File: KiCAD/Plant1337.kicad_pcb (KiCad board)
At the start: 4 copper layers, 59.6 x 48.3 mm, 61 parts, among them J1 USB_C_Receptacle_USB2.0_16P, Q1 AO3400A, Q2 AO3400A, Q3 AO3400A, Q4 AO3400A, U1 SHTC3, U2 ESP32-S3-WROOM-1, U3 AMS1117-3.3

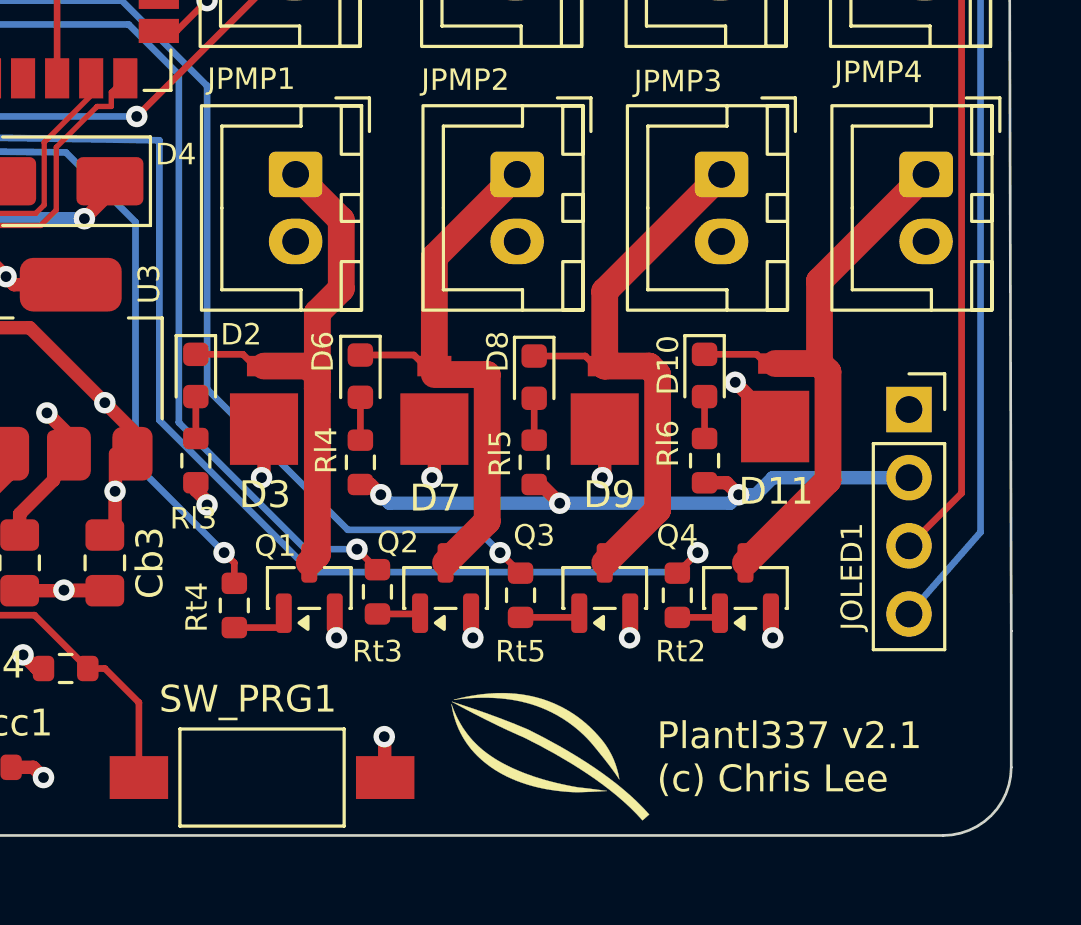
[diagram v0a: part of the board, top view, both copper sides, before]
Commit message: Update PCB layout/schematic: fix flybck diodes
Had wrong footprint
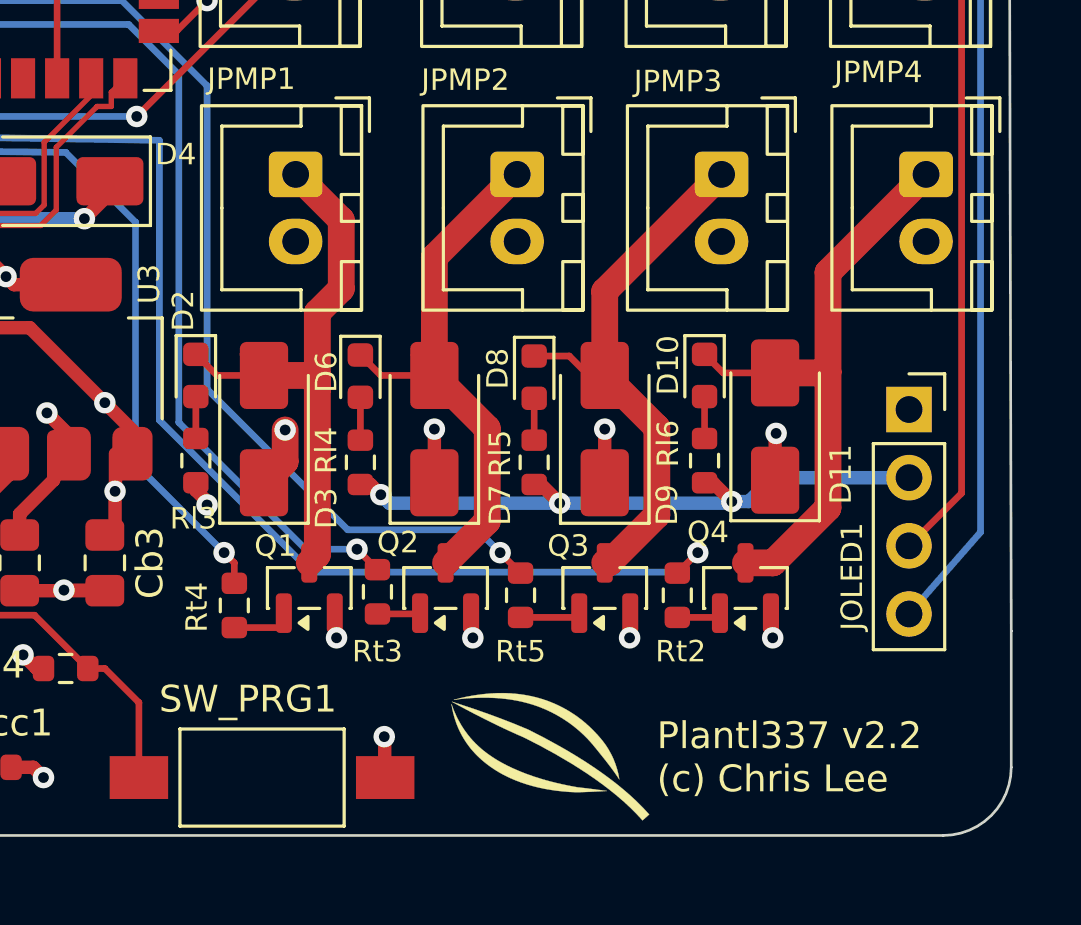
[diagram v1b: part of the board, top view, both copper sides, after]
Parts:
- D11, D3, D7, D9: footprint chl33_library:DO-216 -> Diode_SMD:D_SMA
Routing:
- net JP4: track 22.1 -> 23.7 mm
- net JP1: track 21.2 -> 22.2 mm
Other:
- board text added: "Plantl337 v2.2 (c) Chris Lee"
- board text removed: "Plantl337 v2.1 (c) Chris Lee"
